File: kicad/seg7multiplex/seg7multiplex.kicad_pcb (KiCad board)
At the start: 2 copper layers, 49.5 x 80 mm, 18 parts, among them IC1 ATTINY45-P, J1 USB_A, U1 SN74HC595, U2 SN74HC161, U3 74LS48

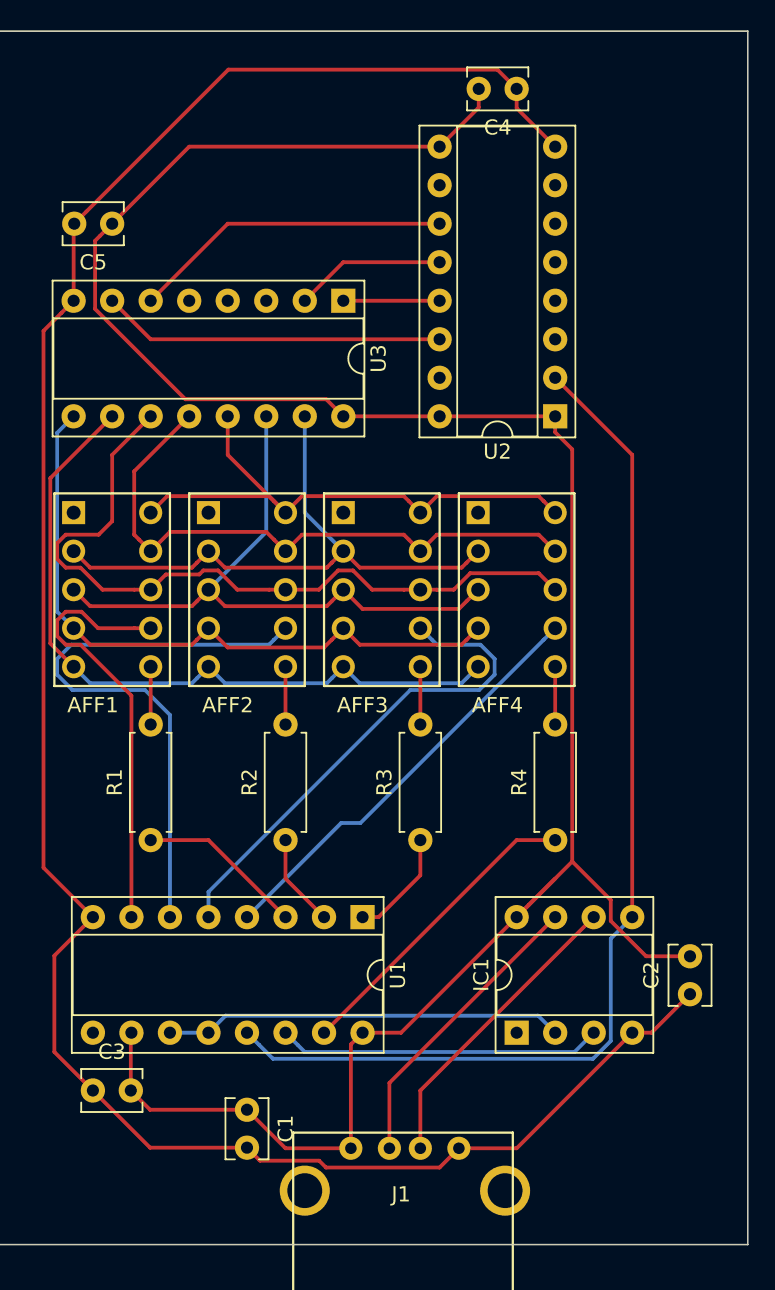
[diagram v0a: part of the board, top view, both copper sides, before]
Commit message: Adjustment after first prototype revision
I've received my first KiCAD-designed PCB! After a few cowboy adjustments
(soldering stuff here and there), I could manage to make the thing work!

But it flickered badly, so I had to heavily optimize my multiplexing
algo to make flickering go away. As it is right now, and with
modification to my KiCAD design (which have been done manually on my
PCB to confirm soundness), I get a display that displays stuff correctly
without flickering!

I have yet to test the serial input. That's the next step before I send
a second revision of the PCB to the fab.

Exciting stuff!
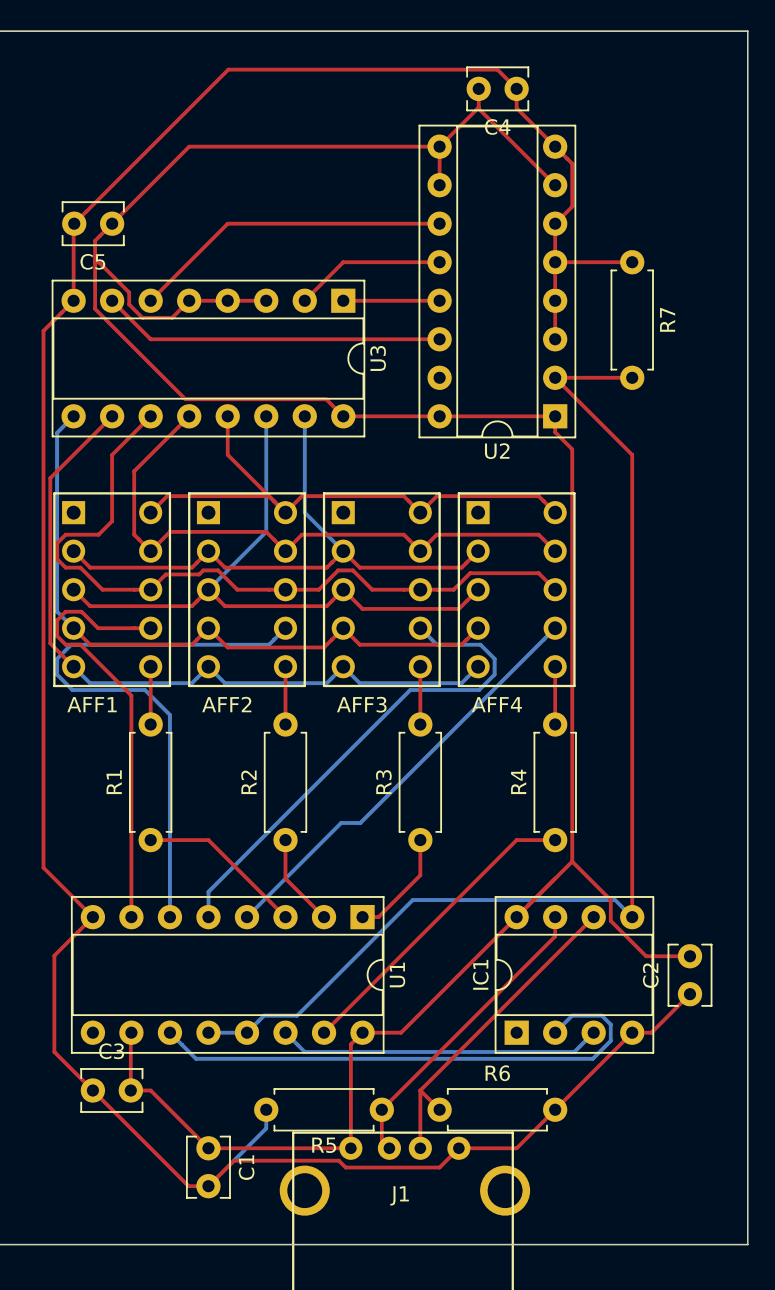
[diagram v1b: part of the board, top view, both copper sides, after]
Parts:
- added R5: 10K, Resistor_THT:R_Axial_DIN0207_L6.3mm_D2.5mm_P7.62mm_Horizontal, F.Cu at (142.2, 116.8)
- added R6: 10K, Resistor_THT:R_Axial_DIN0207_L6.3mm_D2.5mm_P7.62mm_Horizontal, F.Cu at (146.1, 116.8)
- added R7: 10K, Resistor_THT:R_Axial_DIN0207_L6.3mm_D2.5mm_P7.62mm_Horizontal, F.Cu at (158.8, 61.0)
- moved C1 3.59 mm to (130.8, 119.4)
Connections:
- U1 pad 12: Net-(IC1-Pad2) -> /PB0
- U2 pad 10: Net-(U2-Pad10) -> VCC
- U2 pad 3: Net-(U2-Pad3) -> GND
- U2 pad 4: Net-(U2-Pad4) -> GND
- U2 pad 5: Net-(U2-Pad5) -> GND
- U2 pad 6: Net-(U2-Pad6) -> GND
- U2 pad 7: Net-(U2-Pad7) -> VCC
- U3 pad 3: Net-(U3-Pad3) -> VCC
- U3 pad 4: Net-(U3-Pad4) -> VCC
- U3 pad 5: Net-(U3-Pad5) -> VCC
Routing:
- net GND: track 146.4 -> 173.1 mm
- net VCC: track 158.8 -> 182.4 mm
- net Net-(IC1-Pad2): track 26.3 -> 35.7 mm
- net /PB0: track 71.6 -> 74.8 mm
- net /INSER: track 20.0 -> 21.8 mm

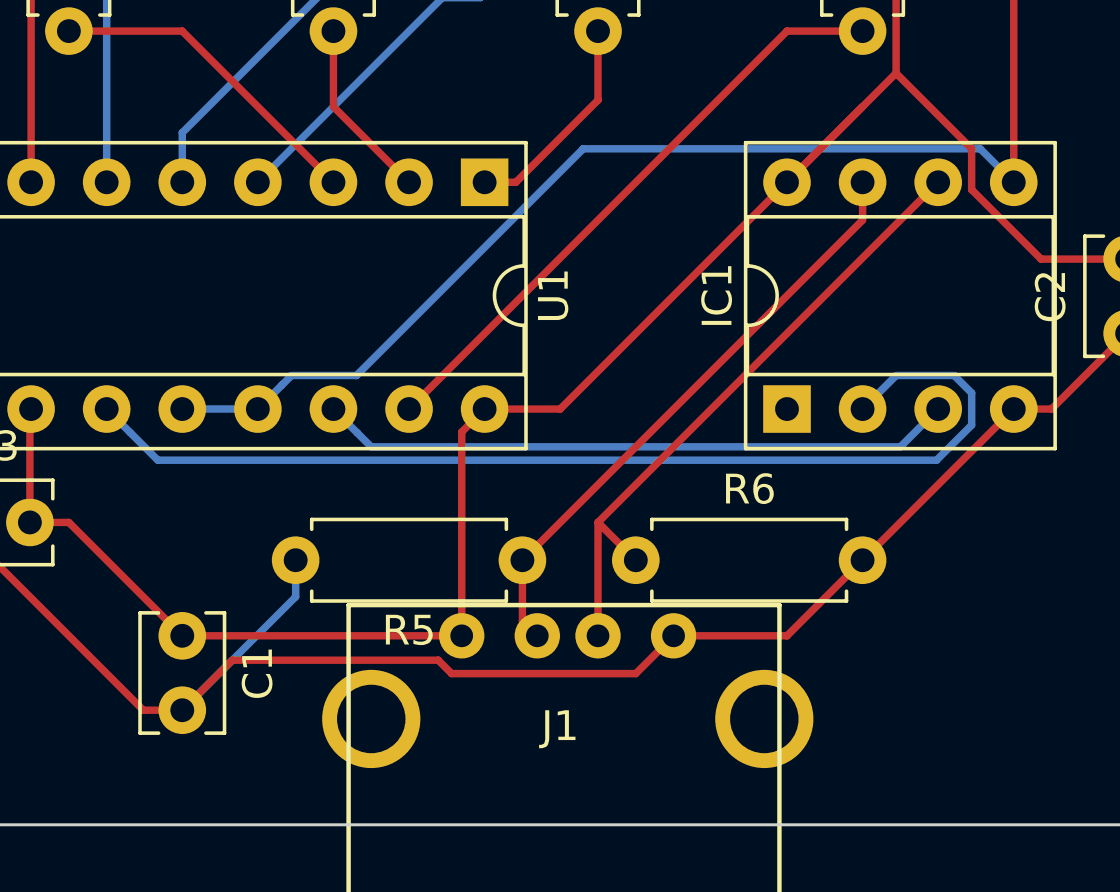
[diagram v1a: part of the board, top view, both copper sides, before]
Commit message: It works perfectly!!!
After some sizeable messing around, I could finally make the prototype
work perfrectly! I mean: the serial protocol works without a hitch, the
proper digits get there 100% of the time! No flickering!

One time cnosuming problem I had was that my FT232H controller I use
for testing has a 5V power supply, but 3V logic (it outputs 3V to its
data pins). It took me a while to realise that. Things weren't working
at all.

To make the prototype compatible with 3V logic, I transformed the
pulldown resistors for INCLK and INSER into pull-up resistor so that the
signal is brought a bit further from the 2.5V threshold between HIGH and
LOW (it brings signal from 2.4V previously to 2.9V now).

Another time consuming problem I had is that I had a bad soldering that
fused PB1 and PB0 together. That took me waaaaay to long to realize
that.

Other than that, I optimized the serial data queue by shrinking it from
16bit to 8 bit to avoid arithmetic operations on 2-bytes variables. 8bit
is enough.

Also, it seems that my digits are now backwards. I don't care much, but
I had to change the simulation to account for that.
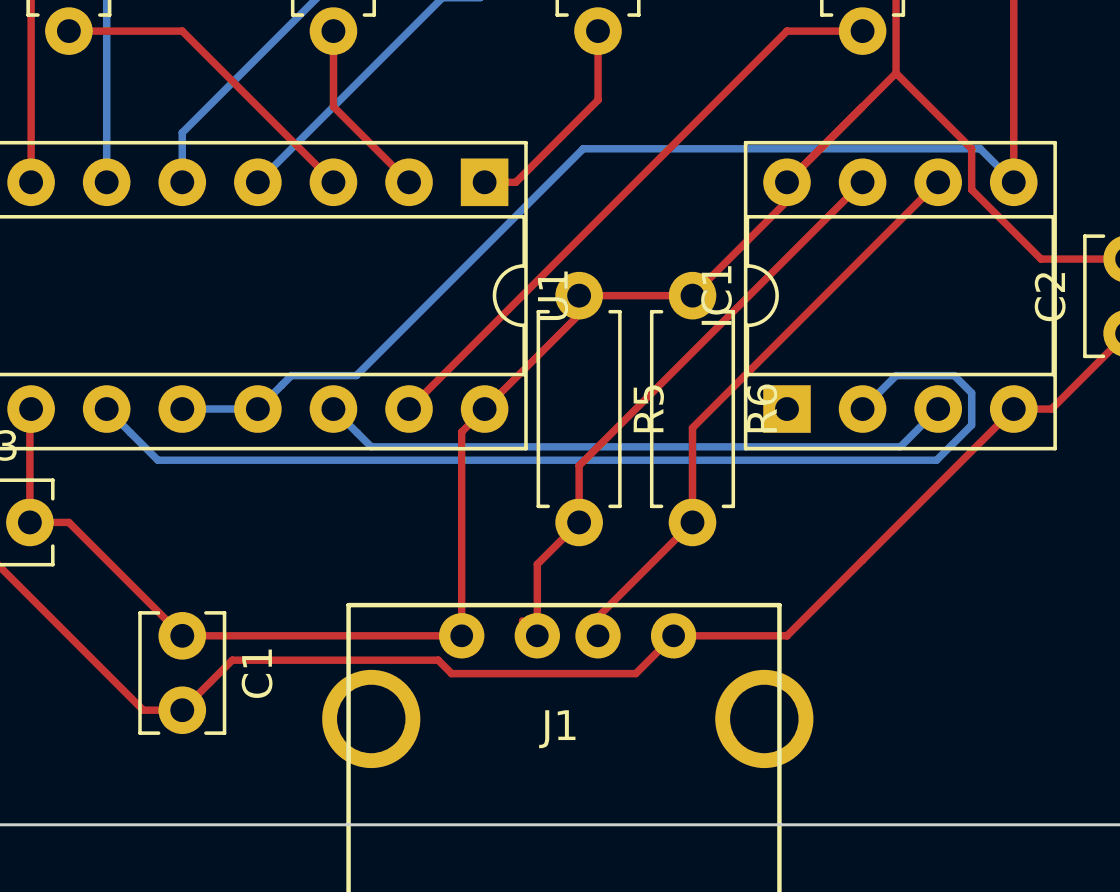
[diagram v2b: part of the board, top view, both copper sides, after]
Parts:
- moved R5 9.09 mm to (144.1, 108.0), turned to 270 degrees
- moved R6 9.09 mm to (148.0, 108.0), turned to 270 degrees
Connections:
- R5 pad 1: /INCLK -> VCC
- R5 pad 2: GND -> /INCLK
- R6 pad 1: /INSER -> VCC
- R6 pad 2: GND -> /INSER
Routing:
- net GND: track 173.1 -> 166.5 mm
- net /INSER: track 21.8 -> 20.0 mm
- net VCC: track 182.4 -> 183.1 mm
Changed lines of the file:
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@@
     (thickness 1.6)
     (drawings 4)
-    (tracks 277)
+    (tracks 280)
     (zones 0)
     (modules 21)
@@
   )
   (module Resistor_THT:R_Axial_DIN0207_L6.3mm_D2.5mm_P7.62mm_Horizontal (layer F.Cu)
-    (at 146.05 116.84)
+    (at 147.955 107.95 270)
     (descr "Resistor, Axial_DIN0207 series, Axial, Horizontal, pin pitch=7.62mm, 0.25W = 1/4W, length*diameter=6.3*2.5mm^2, http://cdn-reichelt.de/documents/datenblatt/B400/1_4W%23YAG.pdf")
     (tags "Resistor Axial_DIN0207 series Axial Horizontal pin pitch 7.62mm 0.25W = 1/4W length 6.3mm diameter 2.5mm")
-    (fp_text reference R6 (at 3.81 -2.37) (layer F.SilkS)
-      (effects (font (size 1 1) (thickness 0.15)))
-    )
-    (fp_text value 10K (at 3.81 2.37) (layer F.Fab)
-      (effects (font (size 1 1) (thickness 0.15)))
-    )
-    (fp_text user %R (at 3.81 0) (layer F.Fab)
+    (fp_text reference R6 (at 3.81 -2.37 270) (layer F.SilkS)
+      (effects (font (size 1 1) (thickness 0.15)))
+    )
+    (fp_text value 10K (at 3.81 2.37 270) (layer F.Fab)
+      (effects (font (size 1 1) (thickness 0.15)))
+    )
+    (fp_text user %R (at 3.81 0 270) (layer F.Fab)
       (effects (font (size 1 1) (thickness 0.15)))
     )
@@
     (fp_line (start 0.66 1.25) (end 6.96 1.25) (layer F.Fab) (width 0.1))
     (fp_line (start 0.66 -1.25) (end 0.66 1.25) (layer F.Fab) (width 0.1))
-    (pad 2 thru_hole oval (at 7.62 0) (size 1.6 1.6) (drill 0.8) (layers *.Cu *.Mask)
-      (net 21 GND))
-    (pad 1 thru_hole circle (at 0 0) (size 1.6 1.6) (drill 0.8) (layers *.Cu *.Mask)
+    (pad 2 thru_hole oval (at 7.62 0 270) (size 1.6 1.6) (drill 0.8) (layers *.Cu *.Mask)
       (net 25 /INSER))
+    (pad 1 thru_hole circle (at 0 0 270) (size 1.6 1.6) (drill 0.8) (layers *.Cu *.Mask)
+      (net 20 VCC))
     (model ${KISYS3DMOD}/Resistor_THT.3dshapes/R_Axial_DIN0207_L6.3mm_D2.5mm_P7.62mm_Horizontal.wrl
       (at (xyz 0 0 0))
@@
   )
   (module Resistor_THT:R_Axial_DIN0207_L6.3mm_D2.5mm_P7.62mm_Horizontal (layer F.Cu)
-    (at 142.24 116.84 180)
+    (at 144.145 107.95 270)
     (descr "Resistor, Axial_DIN0207 series, Axial, Horizontal, pin pitch=7.62mm, 0.25W = 1/4W, length*diameter=6.3*2.5mm^2, http://cdn-reichelt.de/documents/datenblatt/B400/1_4W%23YAG.pdf")
     (tags "Resistor Axial_DIN0207 series Axial Horizontal pin pitch 7.62mm 0.25W = 1/4W length 6.3mm diameter 2.5mm")
-    (fp_text reference R5 (at 3.81 -2.37 180) (layer F.SilkS)
-      (effects (font (size 1 1) (thickness 0.15)))
-    )
-    (fp_text value 10K (at 3.81 2.37 180) (layer F.Fab)
+    (fp_text reference R5 (at 3.81 -2.37 270) (layer F.SilkS)
+      (effects (font (size 1 1) (thickness 0.15)))
+    )
+    (fp_text value 10K (at 3.81 2.37 270) (layer F.Fab)
       (effects (font (size 1 1) (thickness 0.15)))
     )
@@
     (fp_line (start 8.67 1.5) (end 8.67 -1.5) (layer F.CrtYd) (width 0.05))
     (fp_line (start 8.67 -1.5) (end -1.05 -1.5) (layer F.CrtYd) (width 0.05))
-    (fp_text user %R (at 3.81 0 180) (layer F.Fab)
-      (effects (font (size 1 1) (thickness 0.15)))
-    )
-    (pad 1 thru_hole circle (at 0 0 180) (size 1.6 1.6) (drill 0.8) (layers *.Cu *.Mask)
+    (fp_text user %R (at 3.81 0 270) (layer F.Fab)
+      (effects (font (size 1 1) (thickness 0.15)))
+    )
+    (pad 1 thru_hole circle (at 0 0 270) (size 1.6 1.6) (drill 0.8) (layers *.Cu *.Mask)
+      (net 20 VCC))
+    (pad 2 thru_hole oval (at 7.62 0 270) (size 1.6 1.6) (drill 0.8) (layers *.Cu *.Mask)
       (net 27 /INCLK))
-    (pad 2 thru_hole oval (at 7.62 0 180) (size 1.6 1.6) (drill 0.8) (layers *.Cu *.Mask)
-      (net 21 GND))
     (model ${KISYS3DMOD}/Resistor_THT.3dshapes/R_Axial_DIN0207_L6.3mm_D2.5mm_P7.62mm_Horizontal.wrl
       (at (xyz 0 0 0))
@@
   (segment (start 140.2 112.53) (end 140.97 111.76) (width 0.25) (layer F.Cu) (net 20))
   (segment (start 140.2 119.38) (end 140.2 112.53) (width 0.25) (layer F.Cu) (net 20))
-  (segment (start 143.51 111.76) (end 151.13 104.14) (width 0.25) (layer F.Cu) (net 20))
-  (segment (start 140.97 111.76) (end 143.51 111.76) (width 0.25) (layer F.Cu) (net 20))
   (segment (start 151.13 104.14) (end 153.67 101.6) (width 0.25) (layer F.Cu) (net 20))
   (segment (start 151.929999 103.340001) (end 151.13 104.14) (width 0.25) (layer F.Cu) (net 20))
@@
   (segment (start 123.334999 60.96) (end 123.334999 59.545001) (width 0.25) (layer F.Cu) (net 20))
   (segment (start 123.334999 64.040001) (end 123.334999 60.96) (width 0.25) (layer F.Cu) (net 20))
+  (segment (start 144.145 108.585) (end 144.145 107.95) (width 0.25) (layer F.Cu) (net 20))
+  (segment (start 140.97 111.76) (end 144.145 108.585) (width 0.25) (layer F.Cu) (net 20))
+  (segment (start 144.145 107.95) (end 147.955 107.95) (width 0.25) (layer F.Cu) (net 20))
+  (segment (start 151.13 104.775) (end 151.13 104.14) (width 0.25) (layer F.Cu) (net 20))
+  (segment (start 147.955 107.95) (end 151.13 104.775) (width 0.25) (layer F.Cu) (net 20))
   (segment (start 160.02 111.76) (end 162.56 109.22) (width 0.25) (layer F.Cu) (net 21))
   (segment (start 158.75 111.76) (end 160.02 111.76) (width 0.25) (layer F.Cu) (net 21))
@@
   (segment (start 129.5 121.88) (end 123.19 115.57) (width 0.25) (layer F.Cu) (net 21))
   (segment (start 130.81 121.88) (end 129.5 121.88) (width 0.25) (layer F.Cu) (net 21))
-  (segment (start 134.62 118.07) (end 134.62 116.84) (width 0.25) (layer B.Cu) (net 21))
-  (segment (start 130.81 121.88) (end 134.62 118.07) (width 0.25) (layer B.Cu) (net 21))
   (segment (start 158.75 73.66) (end 158.75 104.14) (width 0.25) (layer F.Cu) (net 23))
   (segment (start 153.67 68.58) (end 158.75 73.66) (width 0.25) (layer F.Cu) (net 23))
@@
   (segment (start 154.795001 110.634999) (end 156.750001 110.634999) (width 0.25) (layer B.Cu) (net 24))
   (segment (start 153.67 111.76) (end 154.795001 110.634999) (width 0.25) (layer B.Cu) (net 24))
-  (segment (start 156.21 104.14) (end 144.78 115.57) (width 0.25) (layer F.Cu) (net 25))
-  (segment (start 146.05 116.84) (end 144.78 115.57) (width 0.25) (layer F.Cu) (net 25))
-  (segment (start 144.78 115.57) (end 144.78 119.38) (width 0.25) (layer F.Cu) (net 25))
+  (segment (start 147.955 112.395) (end 147.955 115.57) (width 0.25) (layer F.Cu) (net 25))
+  (segment (start 156.21 104.14) (end 147.955 112.395) (width 0.25) (layer F.Cu) (net 25))
+  (segment (start 144.78 118.745) (end 144.78 119.38) (width 0.25) (layer F.Cu) (net 25))
+  (segment (start 147.955 115.57) (end 144.78 118.745) (width 0.25) (layer F.Cu) (net 25))
   (segment (start 136.689999 112.559999) (end 135.89 111.76) (width 0.25) (layer B.Cu) (net 26))
   (segment (start 137.16 113.03) (end 136.689999 112.559999) (width 0.25) (layer B.Cu) (net 26))
   (segment (start 154.94 113.03) (end 137.16 113.03) (width 0.25) (layer B.Cu) (net 26))
   (segment (start 156.21 111.76) (end 154.94 113.03) (width 0.25) (layer B.Cu) (net 26))
-  (segment (start 153.67 105.41) (end 142.24 116.84) (width 0.25) (layer F.Cu) (net 27))
-  (segment (start 153.67 104.14) (end 153.67 105.41) (width 0.25) (layer F.Cu) (net 27))
   (segment (start 142.24 118.88) (end 142.74 119.38) (width 0.25) (layer F.Cu) (net 27))
-  (segment (start 142.24 116.84) (end 142.24 118.88) (width 0.25) (layer F.Cu) (net 27))
+  (segment (start 144.145 113.665) (end 144.145 115.57) (width 0.25) (layer F.Cu) (net 27))
+  (segment (start 153.67 104.14) (end 144.145 113.665) (width 0.25) (layer F.Cu) (net 27))
+  (segment (start 142.74 116.975) (end 142.74 119.38) (width 0.25) (layer F.Cu) (net 27))
+  (segment (start 144.145 115.57) (end 142.74 116.975) (width 0.25) (layer F.Cu) (net 27))
   (segment (start 130.81 99.06) (end 135.89 104.14) (width 0.25) (layer F.Cu) (net 29))
   (segment (start 127 99.06) (end 130.81 99.06) (width 0.25) (layer F.Cu) (net 29))

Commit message: v3!
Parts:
- removed C4: 0.1uF, Capacitor_THT:C_Disc_D3.8mm_W2.6mm_P2.50mm
- removed R7: 10K, Resistor_THT:R_Axial_DIN0207_L6.3mm_D2.5mm_P7.62mm_Horizontal
- removed U2: SN74HC161, Package_DIP:DIP-16_W7.62mm_Socket
- C1, IC1, R1, R2, R3, R4, U1, U3: moved to B.Cu
- moved C2 84.3 mm to (78.7, 100.3)
- moved J1 83.7 mm to (66.0, 90.2), turned to 270 degrees
- moved R5 77.5 mm to (71.1, 81.9)
- moved R6 77.3 mm to (71.1, 99.7), turned to 90 degrees
- moved C1 71.6 mm to (66.0, 88.9)
- moved IC1 70.5 mm to (82.5, 95.2), turned to 180 degrees
- moved U1 55.3 mm to (86.4, 95.2)
- moved R4 52.5 mm to (101.6, 92.7)
- moved R3 51.8 mm to (93.3, 92.7)
- moved R2 51.2 mm to (85.1, 92.7)
- moved R1 50.6 mm to (76.8, 92.7)
- moved AFF4 49.6 mm to (101.6, 85.0), turned to 270 degrees
- moved AFF3 49.0 mm to (93.3, 85.0), turned to 270 degrees
- moved AFF2 48.4 mm to (85.1, 85.0), turned to 270 degrees
- moved AFF1 47.7 mm to (76.8, 85.0), turned to 270 degrees
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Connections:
- net /PB0 renamed /RCLK
- net Net-(IC1-Pad2) renamed /SRCLK
- AFF1 pad 7: /DP3 -> /SER_DP
- AFF2 pad 7: /DP2 -> /SER_DP
- AFF3 pad 7: /DP1 -> /SER_DP
- AFF4 pad 7: /DP0 -> /SER_DP
- IC1 pad 3: Net-(IC1-Pad3) -> /SER_DP
- R1 pad 1: Net-(R1-Pad1) -> /AFF1
- R1 pad 2: Net-(AFF1-Pad6) -> Net-(AFF1-Pad1)
- R2 pad 1: Net-(R2-Pad1) -> /AFF2
- R2 pad 2: Net-(AFF2-Pad6) -> Net-(AFF2-Pad1)
- R3 pad 1: Net-(R3-Pad1) -> /AFF3
- R3 pad 2: Net-(AFF3-Pad6) -> Net-(AFF3-Pad1)
- R4 pad 1: Net-(R4-Pad1) -> /AFF4
- R4 pad 2: Net-(AFF4-Pad6) -> Net-(AFF4-Pad1)
- U1 pad 1: Net-(R3-Pad1) -> /AFF2
- U1 pad 14: Net-(IC1-Pad3) -> /SER_DP
- U1 pad 15: Net-(R4-Pad1) -> /AFF1
- U1 pad 2: Net-(R2-Pad1) -> /AFF3
- U1 pad 3: Net-(R1-Pad1) -> /AFF4
- U1 pad 4: /DP0 -> /DECA
- U1 pad 5: /DP1 -> /DECB
- U1 pad 6: /DP2 -> /DECC
- U1 pad 7: /DP3 -> /DECD
- U3 pad 1: Net-(U2-Pad13) -> /DECB
- U3 pad 2: Net-(U2-Pad12) -> /DECC
- U3 pad 6: Net-(U2-Pad11) -> /DECD
- U3 pad 7: Net-(U2-Pad14) -> /DECA
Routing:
- net GND: track 166.5 -> 74.8 mm
- net VCC: track 183.1 -> 100.6 mm
- net /SER_DP: track 0.00 -> 62.8 mm
- net /RCLK: track 74.8 -> 23.0 mm
- net /DP2: track 38.8 -> 0.00 mm
- net /DECB: track 0.00 -> 33.3 mm
- net /DP1: track 33.2 -> 0.00 mm
- net /DECC: track 0.00 -> 30.2 mm
- net /DP3: track 29.0 -> 0.00 mm
- net /DP0: track 28.2 -> 0.00 mm
- net /DECA: track 0.00 -> 25.0 mm
- net Net-(U2-Pad14): track 22.6 -> 0.00 mm
- net Net-(IC1-Pad3): track 21.4 -> 0.00 mm
- net Net-(U2-Pad11): track 21.2 -> 0.00 mm
- net Net-(R4-Pad1): track 20.5 -> 0.00 mm
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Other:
- board size 49.5 x 80 mm -> 54.6 x 29.2 mm
